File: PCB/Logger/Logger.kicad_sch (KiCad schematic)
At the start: 74 parts, among them J2 USB-C-Socket-V, J3 JST-PH-SM4-TB, J3 USB-PROG, J5 Conn_01x05, J6 TF_PUSH, J8 Shelly, Q1 C179347, Q4 CJ2301, U1 TP4054, U10 ESP32-S3-MINI-1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

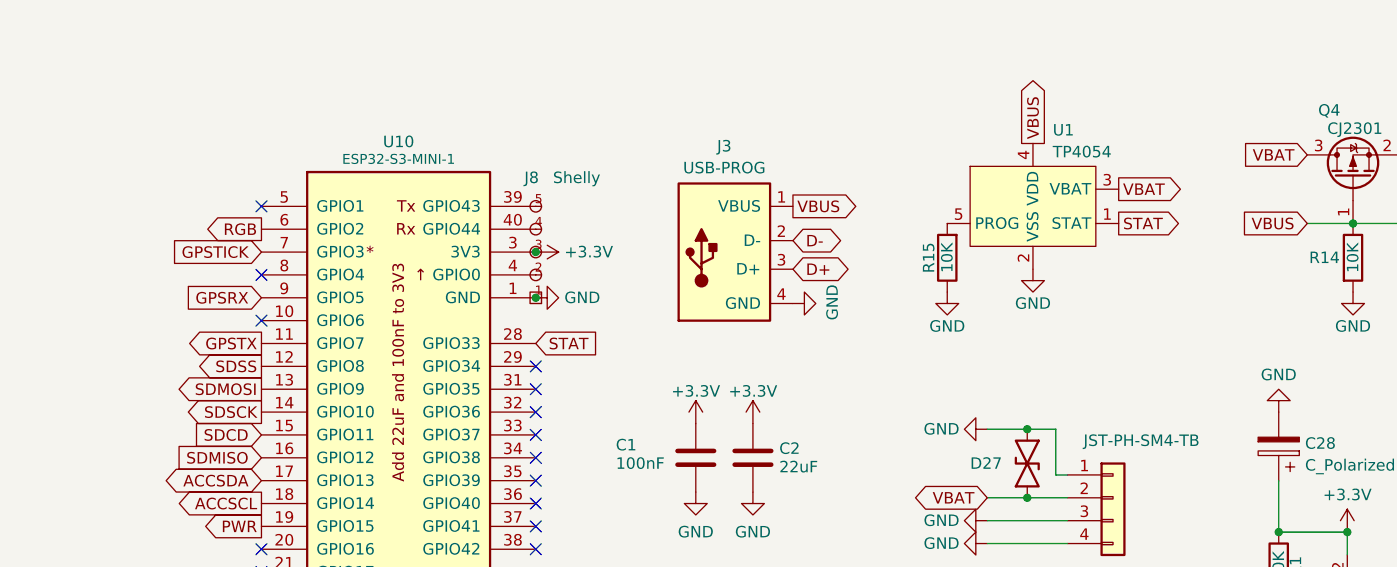
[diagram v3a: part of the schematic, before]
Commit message: Move charger input
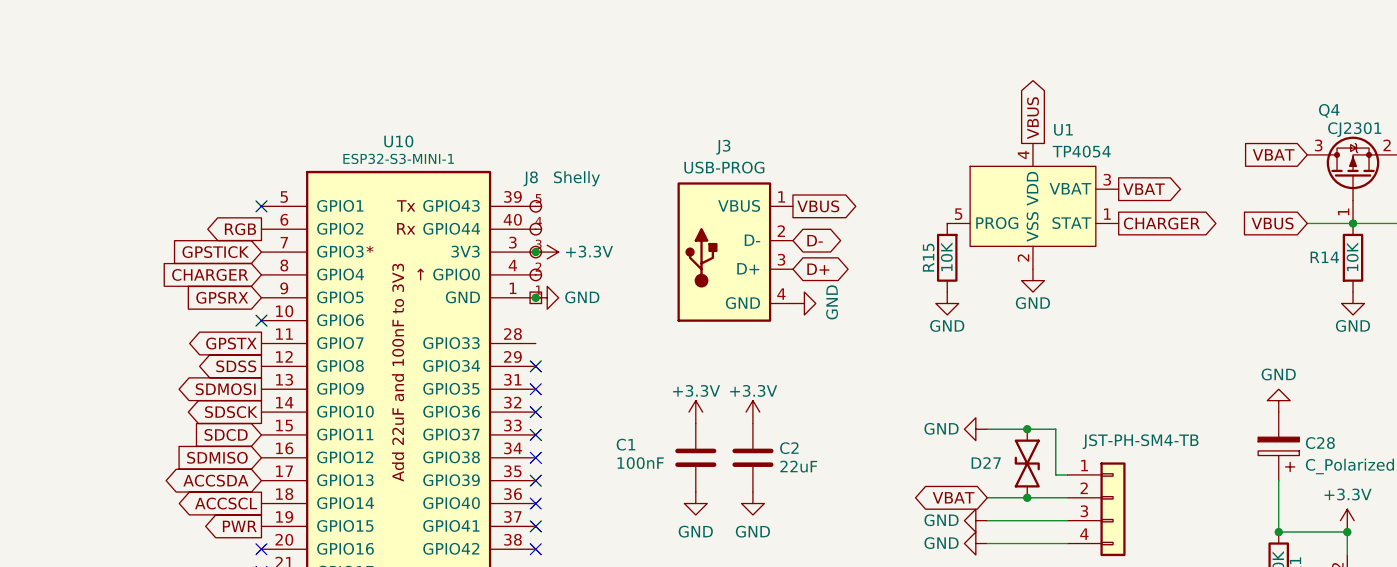
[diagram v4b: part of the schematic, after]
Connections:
- net CHARGER: now reaches U10.8 (GPIO4)
- net CHARGER: now also U1.1 (STAT)
- net STAT: no longer names the net of U10.28 (GPIO33)
- net STAT: no longer U1.1 (STAT)
- no-connect marks 27 -> 26
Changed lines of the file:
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@@
   (no_connect (at 121.92 127.635))
   (no_connect (at 73.025 55.88))
-  (no_connect (at 42.545 43.18))
   (no_connect (at 73.025 78.74))
   (no_connect (at 213.995 114.3))
@@
     (stroke (width 0) (type default))
   )
-  (global_label "STAT" (shape input) (at 73.025 50.8 0) (fields_autoplaced)
-    (effects (font (size 1.27 1.27)) (justify left))
-    (property "Intersheetrefs" "${INTERSHEET_REFS}" (at 79.5893 50.8 0)
-      (effects (font (size 1.27 1.27)) (justify left) hide)
+  (global_label "CHARGER" (shape input) (at 42.545 43.18 180) (fields_autoplaced)
+    (effects (font (size 1.27 1.27)) (justify right))
+    (property "Intersheetrefs" "${INTERSHEET_REFS}" (at 31.5659 43.18 0)
+      (effects (font (size 1.27 1.27)) (justify right) hide)
     )
   )
@@
     )
   )
-  (global_label "STAT" (shape output) (at 137.795 37.465 0) (fields_autoplaced)
+  (global_label "CHARGER" (shape output) (at 137.795 37.465 0) (fields_autoplaced)
     (effects (font (size 1.27 1.27)) (justify left))
-    (property "Intersheetrefs" "${INTERSHEET_REFS}" (at 144.3593 37.465 0)
+    (property "Intersheetrefs" "${INTERSHEET_REFS}" (at 148.7741 37.465 0)
       (effects (font (size 1.27 1.27)) (justify left) hide)
     )
